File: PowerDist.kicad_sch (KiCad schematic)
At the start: 18 parts, among them J18 PowerConn, Q1 NMOS, U12 RI3-1205S, U13 NCP1117-3.3_SOT223

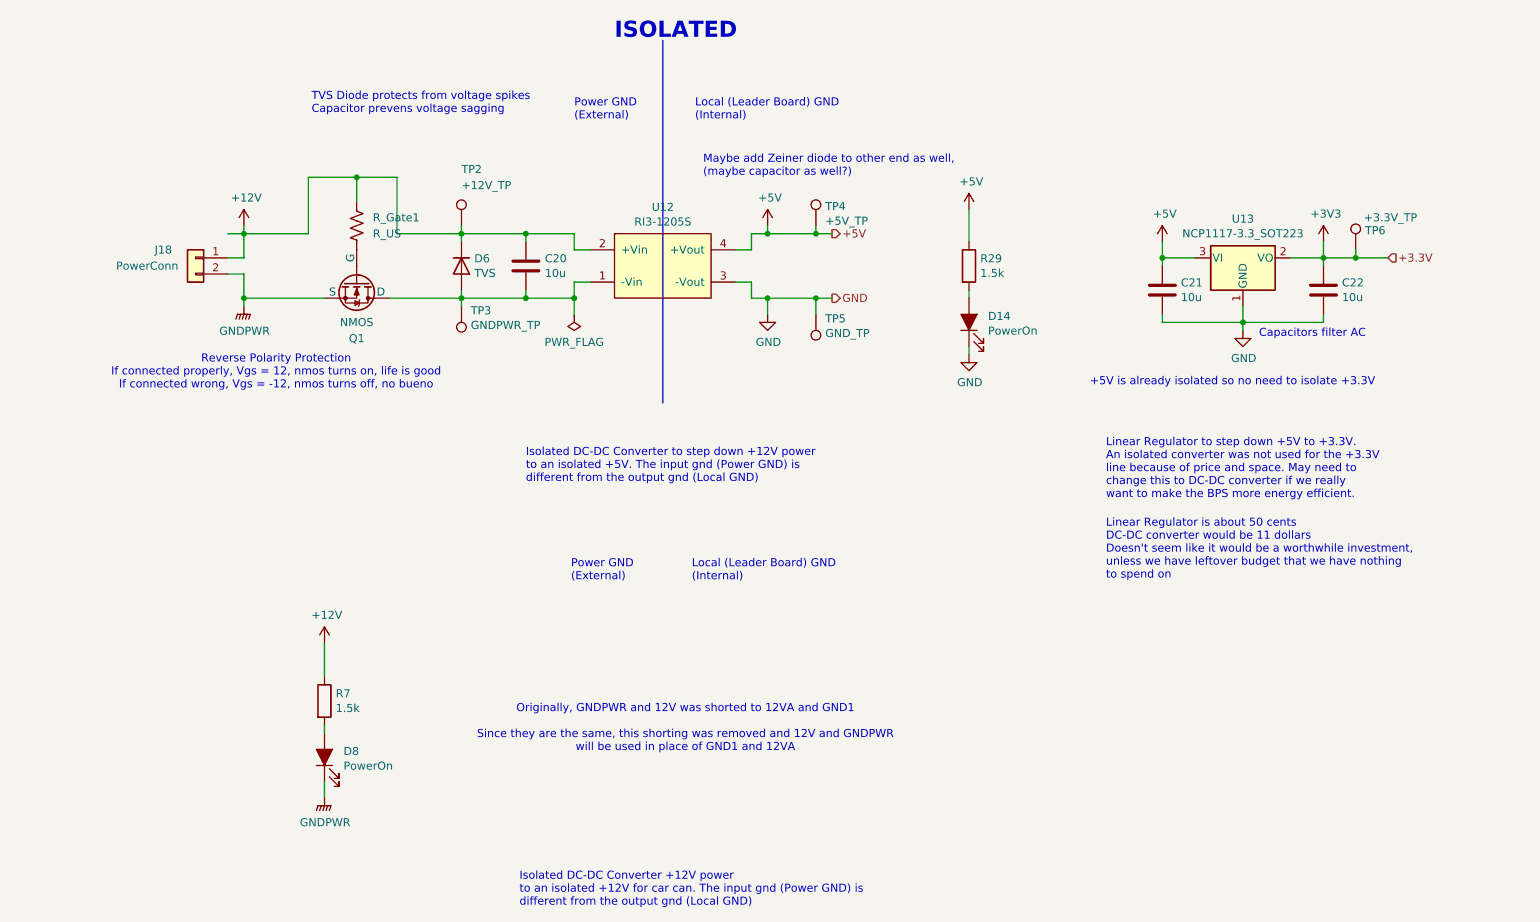
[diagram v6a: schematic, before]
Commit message: Flipped optoisolators, changed resistor values, added second connector to motor can and disconnected shield pins for now since I haven't seen them used (will chack against old version to see what the circuit looked like), copied power-in circuit from contactor board, added optoisolator to timer and blinker light connection.
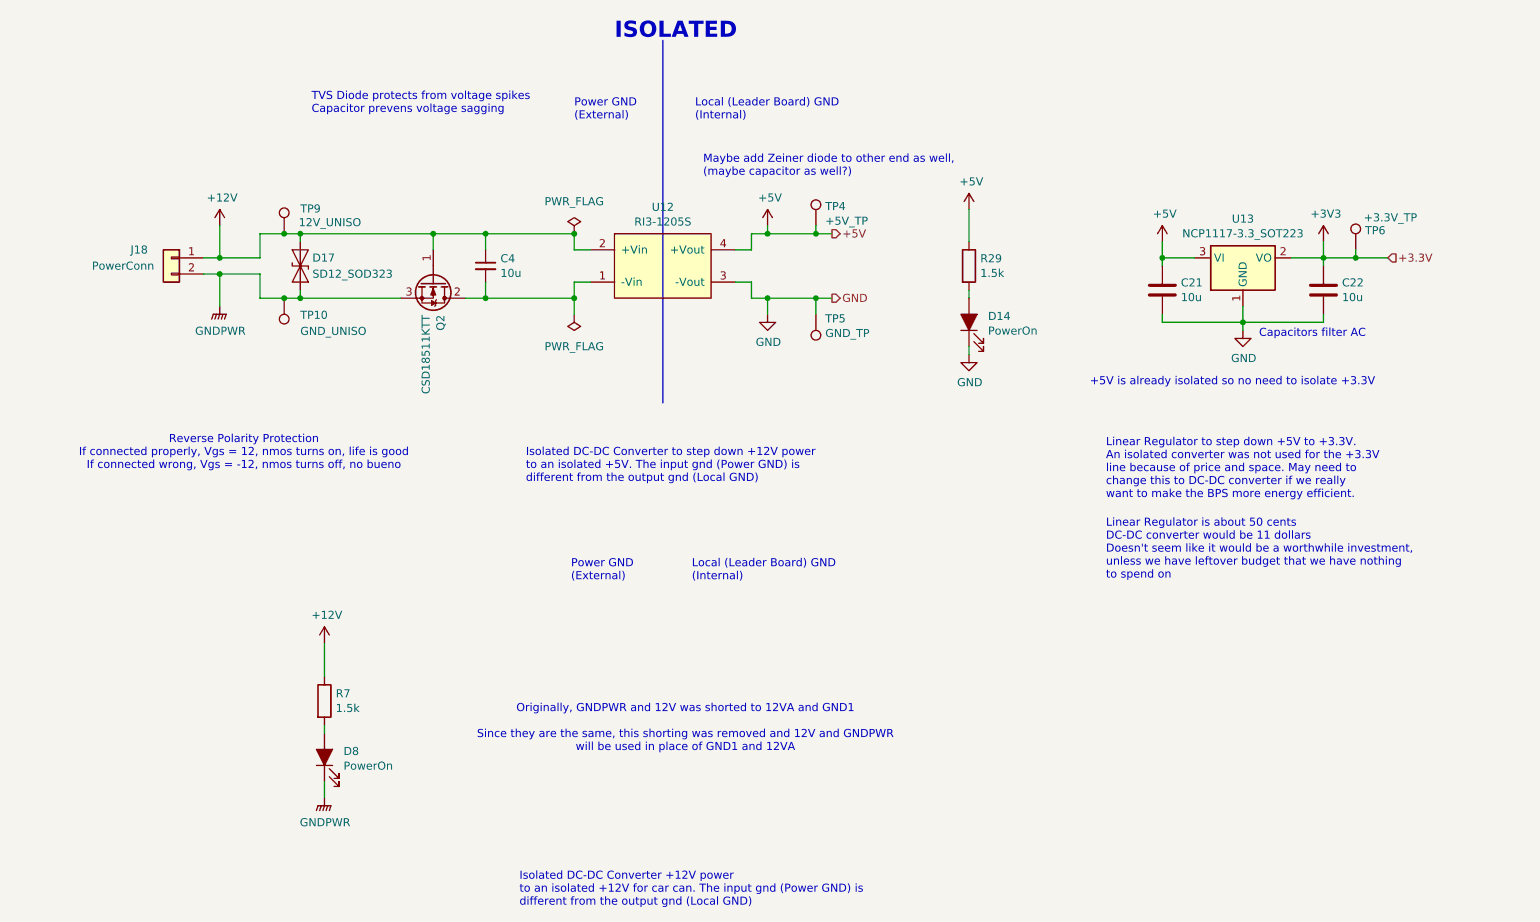
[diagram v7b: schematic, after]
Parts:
- removed C20: 10u, UTSVT_Passive:C_2220_5750Metric, symbol Device:C
- removed D6: TVS, Diode_SMD:D_SOD-323, symbol Device:D
- removed Q1: NMOS, symbol Simulation_SPICE:NMOS
- removed R_Gate1: R_US, symbol Device:R_US
- removed TP2: +12V_TP, TestPoint:TestPoint_Pad_1.5x1.5mm, symbol Connector:TestPoint
- removed TP3: GNDPWR_TP, TestPoint:TestPoint_Pad_1.5x1.5mm, symbol Connector:TestPoint
- added C4: 10u, Capacitor_SMD:C_0805_2012Metric, symbol Device:C_Small
- added D17: SD12_SOD323, Diode_SMD:D_SOD-323, symbol Diode:SD12_SOD323
- added Q2: CSD18511KTT, Package_TO_SOT_SMD:TO-252-2, symbol Device:Q_NMOS_GDS
- added TP10: GND_UNISO, TestPoint:TestPoint_Keystone_5005-5009_Compact, symbol Connector:TestPoint
- added TP9: 12V_UNISO, TestPoint:TestPoint_Keystone_5005-5009_Compact, symbol Connector:TestPoint
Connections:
- net +12V: now also C4.1, D17.2 (A2), Q2.1 (G), TP9.1
- net GNDPWR: now also D17.1 (A1), Q2.3 (S), TP10.1
- net at U12.1 (-Vin): now also C4.2, Q2.2 (D)
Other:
- moved on the sheet: J18

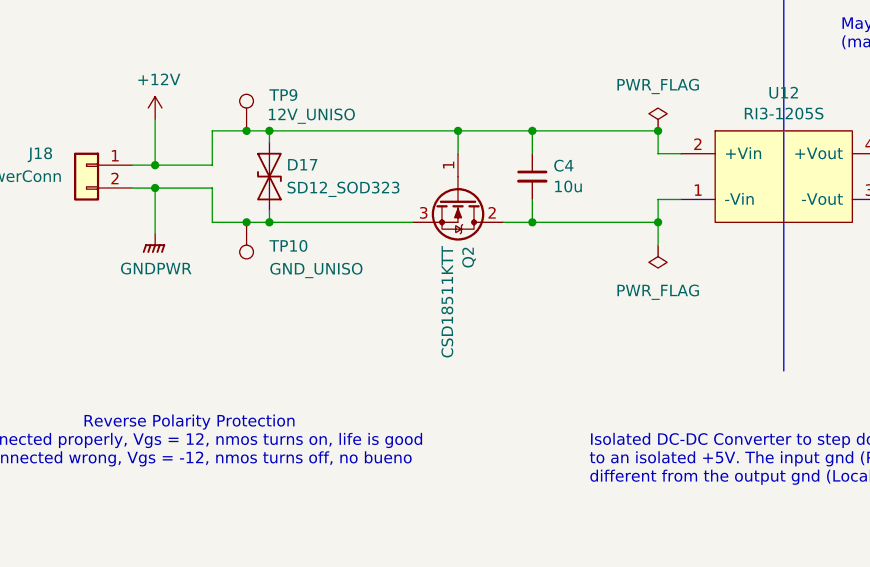
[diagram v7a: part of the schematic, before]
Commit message: Changed names and added power flags until KiCAD ERC was satisfied. Hopefully this did not involve doing anything that wasn't supposed to be done.
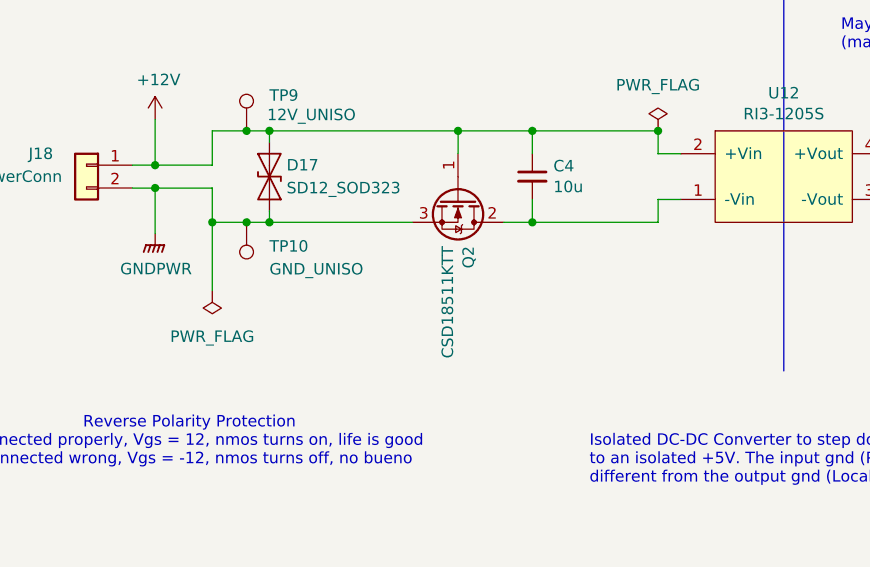
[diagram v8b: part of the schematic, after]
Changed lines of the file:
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@@
-	)
-	(junction
-		(at 99.06 87.63)
-		(diameter 0)
-		(color 0 0 0 0)
 	)
 	(junction
@@
 	)
 	(junction
+		(at 49.53 87.63)
+		(diameter 0)
+		(color 0 0 0 0)
+	)
+	(junction
 		(at 53.34 77.47)
 		(diameter 0)
@@
 	(wire
 		(pts
-			(xy 99.06 87.63) (xy 99.06 90.17)
+			(xy 49.53 87.63) (xy 49.53 95.25)
 		)
 		(stroke
@@
 	(symbol
 		(lib_id "power:PWR_FLAG")
-		(at 99.06 90.17 180)
+		(at 49.53 95.25 180)
 		(unit 1)
 		(exclude_from_sim no)
@@
 		(dnp no)
 		(property "Reference" "#FLG02"
-			(at 99.06 92.075 0)
+			(at 49.53 97.155 0)
 			(effects
 				(font
@@
 		)
 		(property "Value" "PWR_FLAG"
-			(at 99.06 95.25 0)
+			(at 49.53 100.33 0)
 			(effects
 				(font
@@
 		)
 		(property "Footprint" ""
-			(at 99.06 90.17 0)
+			(at 49.53 95.25 0)
 			(effects
 				(font
@@
 		)
 		(property "Datasheet" "~"
-			(at 99.06 90.17 0)
+			(at 49.53 95.25 0)
 			(effects
 				(font
@@
 		)
 		(property "Description" "Special symbol for telling ERC where power comes from"
-			(at 99.06 90.17 0)
-			(effects
-				(font
+			(at 49.53 95.25 0)
+			(effects
+				(font
